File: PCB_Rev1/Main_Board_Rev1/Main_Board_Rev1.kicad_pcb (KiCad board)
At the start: 4 copper layers, 152.4 x 152.4 mm, 84 parts, among them IC1 LT8648SEV#PBF, J1 PRT-14017, J10 B4B-PH-K-S, J11 532610771, J12 532610771, J13 532610771, J2 Conn_01x04_Socket, J3 691137710002, J4 Conn_01x02_Pin, J5 XT60PW-M, J6 Conn_01x02_Pin, J7 Conn_01x02_Pin, J8 Conn_01x02_Pin, J9 B4B-PH-K-S, Q1 AO3400A, Q2 AO3400A, Q3 AO3400A, Q4 IRFHM9331TRPBF, U1 AZ1117IH-3.3TRG1, U2 L298N, X1 B2P-VH, X2 B2P-VH

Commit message: some routing
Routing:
- net 5VEXT: track 199.6 -> 283.0 mm, vias 13 -> 16
- net GND: track 100.8 -> 155.8 mm, vias 7 -> 11
- net 12VEXT: track 9.67 -> 61.3 mm, vias 2 -> 4
- net Net-(J8-Pin_1): track 17.0 -> 44.2 mm, vias 2 -> 4

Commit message: Routing
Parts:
- moved TP-VGSW1 0.90 mm to (25.8, 139.6)
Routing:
- net Net-(IC1-EN/UV): track 62.1 -> 91.2 mm
- net BATT_IN: track 28.2 -> 56.6 mm, vias 2 -> 4
- net Net-(J6-Pin_1): track 4.46 -> 24.5 mm, vias 0 -> 1
- net Net-(C1-Pad1): track 48.4 -> 61.2 mm
- net /CSTAR-Drive/OUT1_MOTOR_1: track 108.6 -> 116.1 mm
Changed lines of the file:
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@@
 	(footprint "TestPoint:TestPoint_Pad_D2.0mm"
 		(layer "F.Cu")
-		(at 25.77 140.49822)
+		(at 25.8 139.6)
 		(descr "SMD pad as test Point, diameter 2.0mm")
 		(tags "test point SMD pad")
@@
 	)
 	(segment
+		(start 26.43572 140.03572)
+		(end 37.77 140.03572)
+		(width 0.2)
+		(layer "F.Cu")
+		(net 1)
+	)
+	(segment
 		(start 52.05856 138.17322)
 		(end 52.23 138.00178)
@@
 	)
 	(segment
+		(start 26 139.6)
+		(end 26.43572 140.03572)
+		(width 0.2)
+		(layer "F.Cu")
+		(net 1)
+	)
+	(segment
+		(start 37.3075 140.49822)
+		(end 37.77 140.03572)
+		(width 0.2)
+		(layer "F.Cu")
+		(net 1)
+	)
+	(segment
+		(start 25.8 139.6)
+		(end 26 139.6)
+		(width 0.2)
+		(layer "F.Cu")
+		(net 1)
+	)
+	(segment
 		(start 40 136)
 		(end 40 140)
@@
 	)
 	(segment
+		(start 111.799976 157.070108)
+		(end 101.299976 157.070108)
+		(width 0.2)
+		(layer "F.Cu")
+		(net 5)
+	)
+	(segment
+		(start 111.799976 157.070108)
+		(end 93.212476 157.070108)
+		(width 0.2)
+		(layer "F.Cu")
+		(net 5)
+	)
+	(segment
 		(start 88.81285 151.819919)
 		(end 88.192276 151.819919)
@@
 	)
 	(segment
-		(start 88.5 150.5)
-		(end 88.372735 150.5)
+		(start 93.212476 157.070108)
+		(end 92.799976 157.482608)
 		(width 0.2)
 		(layer "F.Cu")
@@
 	)
 	(segment
-		(start 93.212476 157.070108)
-		(end 92.799976 157.482608)
+		(start 88.5 150.5)
+		(end 88.372735 150.5)
 		(width 0.2)
 		(layer "F.Cu")
@@
 	)
 	(segment
+		(start 85.05 104.85)
+		(end 85.05 106.5625)
+		(width 0.2)
+		(layer "F.Cu")
+		(net 8)
+	)
+	(segment
+		(start 82.5 96.5625)
+		(end 82.5 101.9)
+		(width 0.2)
+		(layer "F.Cu")
+		(net 8)
+	)
+	(segment
+		(start 82.5 101.9)
+		(end 82.4 102)
+		(width 0.2)
+		(layer "F.Cu")
+		(net 8)
+	)
+	(segment
+		(start 82.4 102)
+		(end 82.4 102.2)
+		(width 0.2)
+		(layer "F.Cu")
+		(net 8)
+	)
+	(segment
 		(start 83.7 107.9125)
 		(end 85.05 106.5625)
@@
 	)
 	(segment
+		(start 82.4 102.2)
+		(end 85.05 104.85)
+		(width 0.2)
+		(layer "F.Cu")
+		(net 8)
+	)
+	(via
+		(at 82.4 102)
+		(size 0.6)
+		(drill 0.3)
+		(layers "F.Cu" "B.Cu")
+		(net 8)
+	)
+	(segment
+		(start 82.4 102)
+		(end 73.5 102)
+		(width 0.2)
+		(layer "B.Cu")
+		(net 8)
+	)
+	(segment
 		(start 97.45 29.95)
 		(end 97.45 25.4)
@@
 	)
 	(segment
+		(start 47.4 147)
+		(end 47.27 146.87)
+		(width 0.2)
+		(layer "F.Cu")
+		(net 36)
+	)
+	(segment
 		(start 59.5 146.5)
 		(end 59.6 146.6)
@@
 	)
 	(segment
+		(start 30.2 147)
+		(end 26 147)
+		(width 0.2)
+		(layer "F.Cu")
+		(net 36)
+	)
+	(segment
 		(start 52.057 139.99822)
 		(end 52.057 138.66726)
@@
 		(net 36)
 	)
+	(segment
+		(start 47.27 146.87)
+		(end 47.27 139.99822)
+		(width 0.2)
+		(layer "F.Cu")
+		(net 36)
+	)
+	(via
+		(at 30.2 147)
+		(size 0.6)
+		(drill 0.3)
+		(layers "F.Cu" "B.Cu")
+		(net 36)
+	)
 	(via
 		(at 52 146.5)
@@
 		(net 36)
 	)
+	(via
+		(at 47.4 147)
+		(size 0.6)
+		(drill 0.3)
+		(layers "F.Cu" "B.Cu")
+		(net 36)
+	)
+	(segment
+		(start 30.2 147)
+		(end 47.4 147)
+		(width 0.2)
+		(layer "B.Cu")
+		(net 36)
+	)
 	(segment
 		(start 59.6 146.6)
@@
 		(width 0.2)
 		(layer "F.Cu")
+		(net 42)
+	)
+	(segment
+		(start 79 53.5)
+		(end 79 60.96)
+		(width 0.2)
+		(layer "F.Cu")

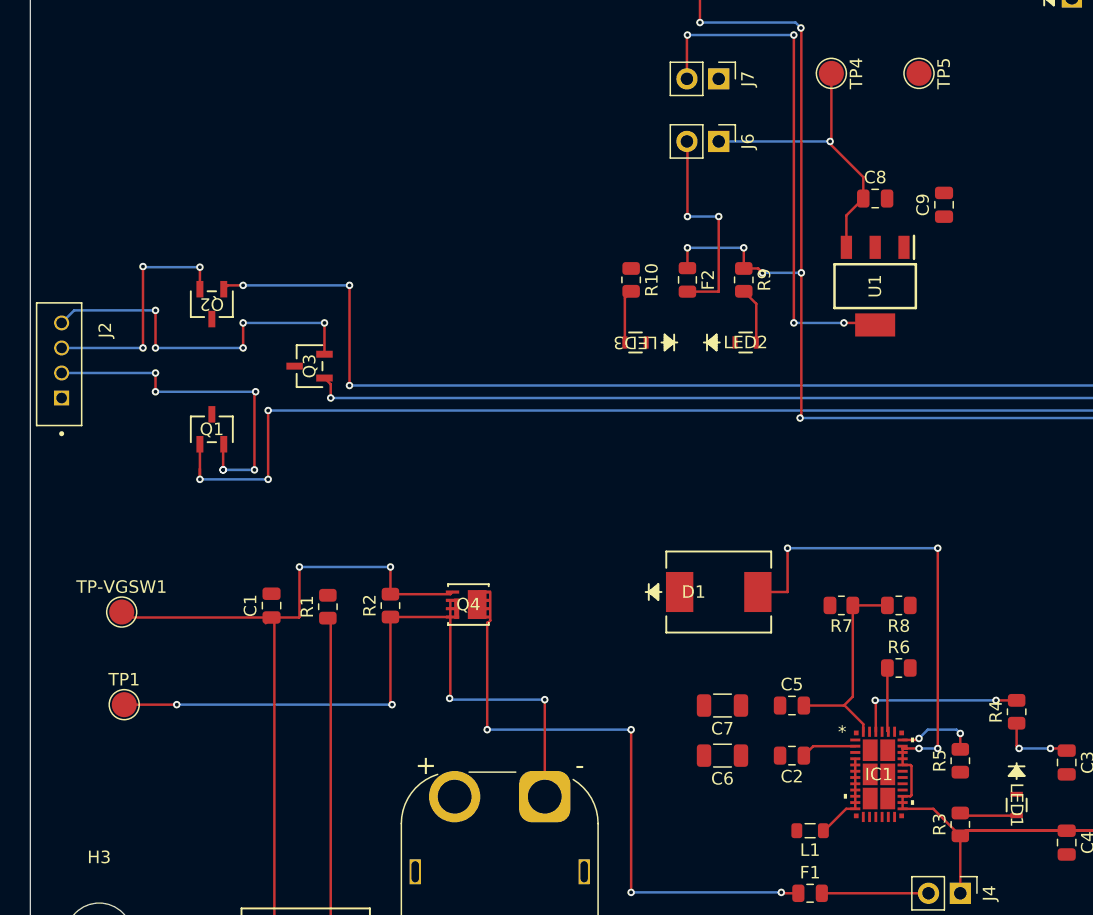
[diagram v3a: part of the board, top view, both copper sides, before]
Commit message: main board routing
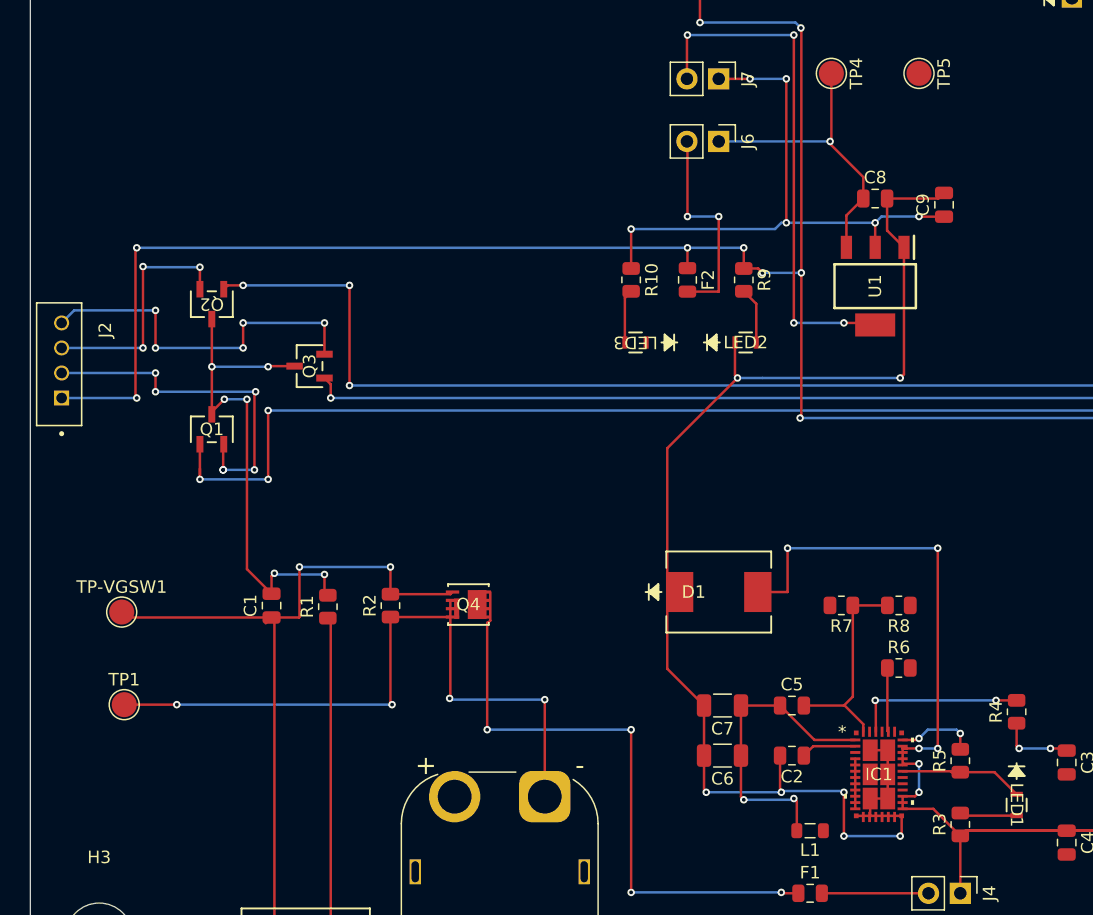
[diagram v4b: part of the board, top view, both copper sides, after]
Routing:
- net GND: track 155.8 -> 316.0 mm, vias 11 -> 24
- net 5VEXT: track 283.0 -> 345.1 mm, vias 16 -> 18
- net +3V3: track 108.5 -> 155.9 mm, vias 5 -> 11
- net 12VEXT: track 61.3 -> 85.9 mm, vias 4 -> 6
- net Net-(IC1-SW_1): track 7.27 -> 4.07 mm
- net Net-(IC1-EN/UV): track 91.2 -> 92.5 mm, vias 4 -> 6

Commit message: Mainboard finished traces
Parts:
- moved TP3 50.0 mm to (62.5, 142.5)
- moved TP4 2.56 mm to (82.5, 94.0)
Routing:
- net 12VEXT: track 85.9 -> 301.8 mm, vias 6 -> 20
- net +3V3: track 155.9 -> 241.2 mm, vias 11 -> 14
- net GND: track 316.0 -> 365.9 mm, vias 24 -> 32
- net Net-(IC1-EN/UV): track 92.5 -> 74.6 mm, vias 6 -> 8
- net Net-(IC1-SW_1): track 4.07 -> 9.50 mm, vias 0 -> 2
- net BATT_IN: track 56.6 -> 53.5 mm, vias 4 -> 3
- net Net-(J6-Pin_1): track 24.5 -> 27.1 mm
- net /CSTAR-Drive/OUT2_MOTOR_1: track 144.7 -> 142.9 mm
- net RGB_Red_Control: track 180.6 -> 179.7 mm
- net 5VEXT: track 345.1 -> 345.0 mm, vias 18 -> 17
- net Net-(PS1-SW): vias 2 -> 0
- net Net-(IC1-INTVCC): vias 0 -> 2
- net GPIO2: vias 2 -> 3
- net GPIO13: vias 5 -> 3
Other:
- outline, holes or cut-outs redrawn

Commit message: how do you polygon
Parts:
- moved R1 2.83 mm to (42.3, 142.0)
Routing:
- net GND: track 365.9 -> 358.4 mm, vias 32 -> 31
- net Net-(J3-Pad1): track 27.7 -> 25.6 mm
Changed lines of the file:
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@@
 	(footprint "Resistor_SMD:R_0805_2012Metric"
 		(layer "F.Cu")
-		(at 42.27 139.17322 90)
+		(at 42.27 142 90)
 		(descr "Resistor SMD 0805 (2012 Metric), square (rectangular) end terminal, IPC_7351 nominal, (Body size source: IPC-SM-782 page 72, https://www.pcb-3d.com/wordpress/wp-content/uploads/ipc-sm-782a_amendment_1_and_2.pdf), generated with kicad-footprint-generator")
 		(tags "resistor")
@@
 	)
 	(segment
-		(start 37.77 136.73)
-		(end 38 136.5)
-		(width 0.2)
-		(layer "F.Cu")
-		(net 2)
-	)
-	(segment
 		(start 35.8055 136.17122)
 		(end 37.77 138.13572)
@@
 	)
 	(segment
-		(start 37.77 138.13572)
-		(end 37.77 136.73)
-		(width 0.2)
-		(layer "F.Cu")
-		(net 2)
-	)
-	(segment
 		(start 134 149.5)
 		(end 134 150.5)
@@
 	)
 	(segment
-		(start 42 137.99072)
-		(end 42.27 138.26072)
-		(width 0.2)
-		(layer "F.Cu")
-		(net 2)
-	)
-	(segment
 		(start 72.324976 151.070108)
 		(end 72.324976 153.824976)
@@
 	)
 	(segment
-		(start 42 136.6)
-		(end 42 137.99072)
-		(width 0.2)
-		(layer "F.Cu")
-		(net 2)
-	)
-	(segment
 		(start 89 149)
 		(end 89.648532 149)
@@
 	)
 	(via
-		(at 42 136.6)
+		(at 43 138.5)
 		(size 0.6)
 		(drill 0.3)
@@
 		(net 2)
 	)
-	(via
-		(at 38 136.5)
-		(size 0.6)
-		(drill 0.3)
-		(layers "F.Cu" "B.Cu")
-		(net 2)
-	)
 	(segment
 		(start 99 28.4)
@@
 	)
 	(segment
-		(start 38 136.5)
-		(end 38.1 136.6)
-		(width 0.2)
-		(layer "B.Cu")
-		(net 2)
-	)
-	(segment
 		(start 88 157.5)
 		(end 83.5 157.5)
@@
 	)
 	(segment
-		(start 38.1 136.6)
-		(end 42 136.6)
-		(width 0.2)
-		(layer "B.Cu")
-		(net 2)
-	)
-	(segment
 		(start 73.5 80)
 		(end 60 80)
@@
 	)
 	(segment
-		(start 42.5 167)
-		(end 42.5 140.31572)
+		(start 43 167.5)
+		(end 42.5 167)
 		(width 0.2)
 		(layer "F.Cu")
@@
 	)
 	(segment
-		(start 43 167.5)
-		(end 42.5 167)
+		(start 43 143.6425)
+		(end 42.27 142.9125)
 		(width 0.2)
 		(layer "F.Cu")
@@
 	)
 	(segment
-		(start 42.5 140.31572)
-		(end 42.27 140.08572)
+		(start 43 167.5)
+		(end 43 143.6425)
 		(width 0.2)
 		(layer "F.Cu")

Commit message: poly shit
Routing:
- net GND: track 358.4 -> 360.0 mm
- added copper zone on F.Cu, net GND
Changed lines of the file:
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@@
 	)
 	(segment
+		(start 42.5 140.81375)
+		(end 42.5 139.18625)
+		(width 0.508)
+		(layer "F.Cu")
+		(net 2)
+	)
+	(segment
 		(start 35.8055 136.17122)
 		(end 37.77 138.13572)
@@
 	)
 	(via
-		(at 43 138.5)
+		(at 42.5 139.18625)
 		(size 0.6)
 		(drill 0.3)
@@
 	)
 	(zone
+		(net 2)
+		(net_name "GND")
+		(layer "F.Cu")
+		(hatch full 0.5)
+		(priority 1)
+		(connect_pads yes
+			(clearance 0.5)
+		)
+		(min_thickness 0.25)
+		(filled_areas_thickness no)
+		(fill yes
+			(thermal_gap 0.5)
+			(thermal_bridge_width 0.5)
+		)
+		(polygon
+			(pts
+				(xy 42 140) (xy 42.5 140) (xy 43 141) (xy 41.5 141)
+			)
+		)
+	)
+	(zone

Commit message: Routing
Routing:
- net GND: track 360.0 -> 358.4 mm
- net Net-(C1-Pad1): track 61.2 -> 60.3 mm
- net BATT_IN: track 53.5 -> 52.8 mm
- removed copper zone on F.Cu, net GND
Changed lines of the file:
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@@
 	)
 	(segment
-		(start 40 140)
-		(end 39.96428 140.03572)
+		(start 47.27 138.17322)
+		(end 52.05856 138.17322)
 		(width 0.2)
 		(layer "F.Cu")
@@
 	)
 	(segment
-		(start 47.27 138.17322)
-		(end 52.05856 138.17322)
+		(start 26.43572 140.03572)
+		(end 37.77 140.03572)
 		(width 0.2)
 		(layer "F.Cu")
@@
 	)
 	(segment
-		(start 26.43572 140.03572)
+		(start 39.56428 140.03572)
 		(end 37.77 140.03572)
 		(width 0.2)
@@
 	)
 	(segment
-		(start 37.3075 140.49822)
-		(end 37.77 140.03572)
-		(width 0.2)
-		(layer "F.Cu")
-		(net 1)
-	)
-	(segment
 		(start 25.8 139.6)
 		(end 26 139.6)
@@
 	)
 	(segment
-		(start 40 136)
-		(end 40 140)
+		(start 38 140.26572)
+		(end 37.77 140.03572)
 		(width 0.2)
 		(layer "F.Cu")
@@
 	)
 	(segment
-		(start 38 140.26572)
-		(end 37.77 140.03572)
+		(start 40 139.6)
+		(end 39.56428 140.03572)
 		(width 0.2)
 		(layer "F.Cu")
@@
 	)
 	(segment
-		(start 38 167.5)
-		(end 38 140.26572)
+		(start 40 136)
+		(end 40 139.6)
 		(width 0.2)
 		(layer "F.Cu")
@@
 	)
 	(segment
-		(start 39.96428 140.03572)
-		(end 37.77 140.03572)
+		(start 38 167.5)
+		(end 38 140.26572)
 		(width 0.2)
 		(layer "F.Cu")
@@
 	)
 	(segment
-		(start 42.5 140.81375)
-		(end 42.5 139.18625)
-		(width 0.508)
-		(layer "F.Cu")
-		(net 2)
-	)
-	(segment
 		(start 35.8055 136.17122)
 		(end 37.77 138.13572)
@@
 	)
 	(segment
-		(start 59.6 154.35)
-		(end 59.6 146.6)
-		(width 0.2)
-		(layer "F.Cu")
-		(net 36)
-	)
-	(segment
 		(start 47.4 147)
 		(end 47.27 146.87)
@@
 	)
 	(segment
-		(start 59.5 146.5)
-		(end 59.6 146.6)
+		(start 30.2 147)
+		(end 26 147)
 		(width 0.2)
 		(layer "F.Cu")
@@
 	)
 	(segment
-		(start 30.2 147)
-		(end 26 147)
+		(start 59.6 154.35)
+		(end 59.6 147)
 		(width 0.2)
 		(layer "F.Cu")
@@
 	)
 	(via
-		(at 59.6 146.6)
+		(at 59.6 147)
 		(size 0.6)
 		(drill 0.3)
@@
 	)
 	(segment
-		(start 59.6 146.6)
-		(end 52.1 146.6)
-		(width 0.2)
-		(layer "B.Cu")
-		(net 36)
-	)
-	(segment
-		(start 52.1 146.6)
-		(end 51.7 147)
-		(width 0.2)
-		(layer "B.Cu")
-		(net 36)
-	)
-	(segment
-		(start 51.7 147)
+		(start 59.6 147)
 		(end 47.4 147)
 		(width 0.2)
@@
 	)
 	(zone
-		(net 2)
-		(net_name "GND")
-		(layer "F.Cu")
-		(hatch full 0.5)
-		(priority 1)
-		(connect_pads yes
-			(clearance 0.5)
-		)
-		(min_thickness 0.25)
-		(filled_areas_thickness no)
-		(fill yes
-			(thermal_gap 0.5)
-			(thermal_bridge_width 0.5)
-		)
-		(polygon
-			(pts
-				(xy 42 140) (xy 42.5 140) (xy 43 141) (xy 41.5 141)
-			)
-		)
-	)
-	(zone
